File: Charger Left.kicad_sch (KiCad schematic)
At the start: 6 parts, among them Q1 AO4459, U1 CN3702

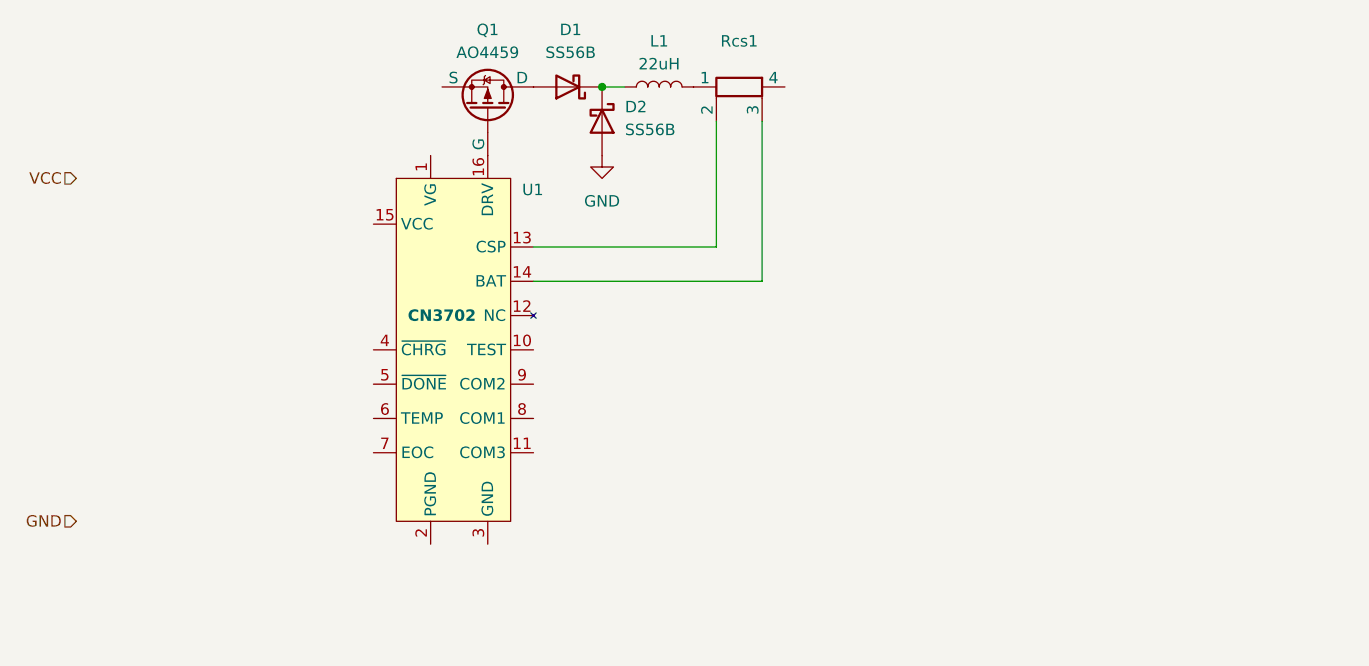
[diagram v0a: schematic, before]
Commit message: Add some resistors and caps
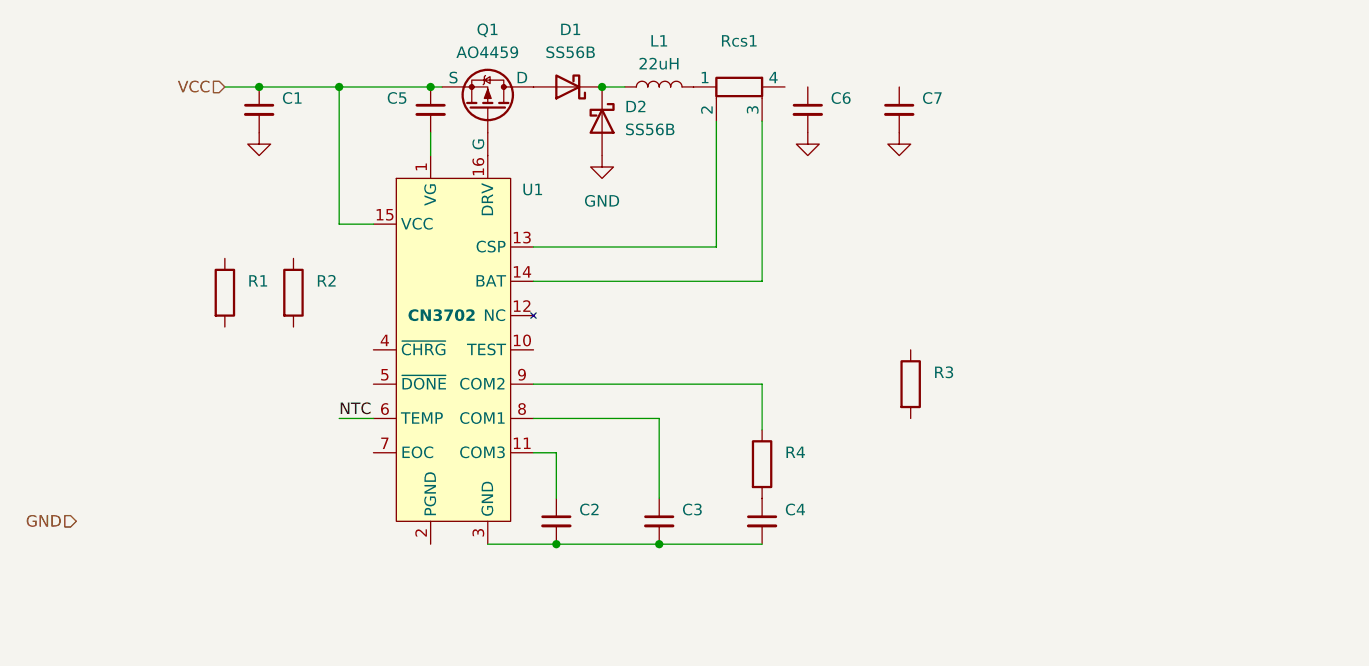
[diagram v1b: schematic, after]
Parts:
- added C1, C2, C3, C4, C5, C6, C7: (no value), symbol Device:C_Small
- added R1, R2, R3, R4: (no value), symbol Device:R
- Rcs1: footprint (none) -> BRAUNIT Charger:R_Shunt_2010_5025Metric
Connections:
- net GND: now also C1.2, C6.2, C7.2
- net VCC: now also Q1.1 (S), Q1.2 (S), Q1.3 (S), U1.15 (VCC), C1.1, C5.1
- net at U1.1 (VG): now also C5.2
- net at U1.11 (COM3): now also C2.1
- net at U1.3 (GND): now also C2.2, C3.2, C4.2
- net NTC: now reaches U1.6 (TEMP)
- net at U1.8 (COM1): now also C3.1
- net at U1.9 (COM2): now also R4.1
- new net: C4.1, R4.2

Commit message: Add BRAUNIT connector and battery detect/charge enable
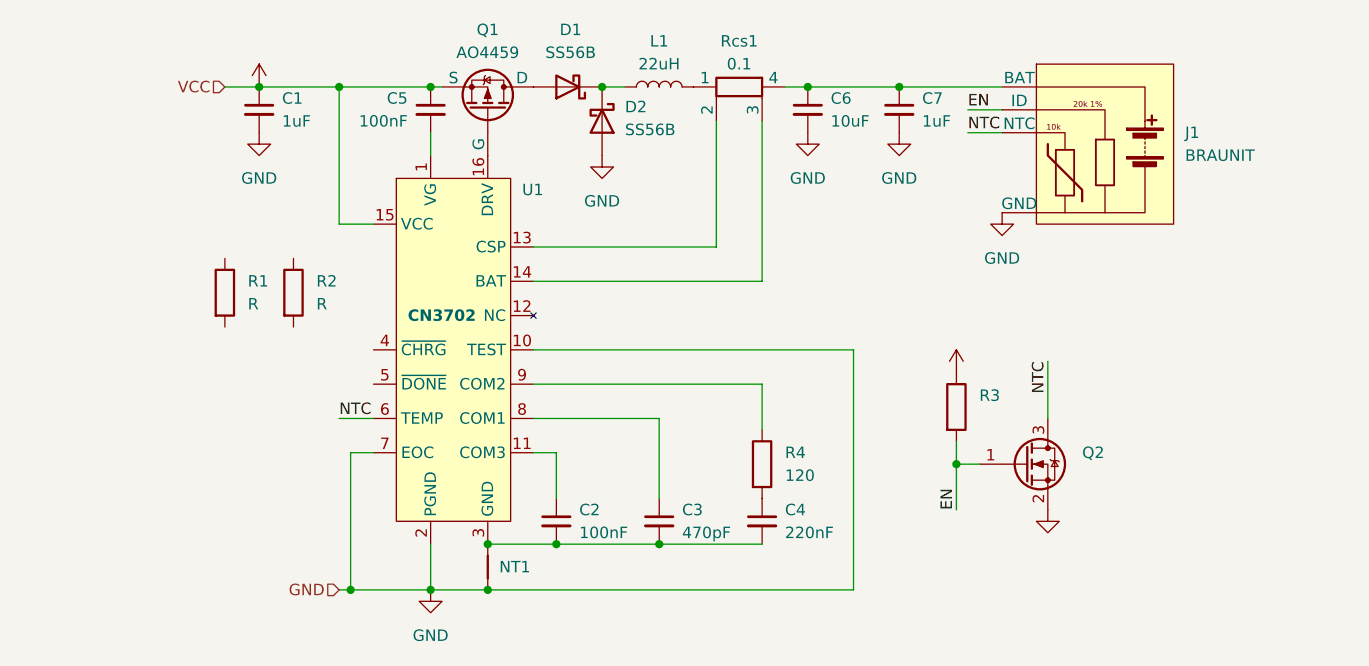
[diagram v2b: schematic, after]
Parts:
- added J1: BRAUNIT, BRAUNIT Charger:Blade_1x04_P2.5mm_Vertical_BRAUNIT_Loose, symbol BRAUNIT Charger:BRAUNIT
- added NT1: NetTie_2, NetTie:NetTie-2_SMD_Pad0.5mm, symbol Device:NetTie_2
- added Q2: (no value), symbol Transistor_FET:2N7002
- C1, C7: value (none) -> 1uF; footprint (none) -> Capacitor_SMD:C_0805_2012Metric
- C2, C5: value (none) -> 100nF; footprint (none) -> Capacitor_SMD:C_0805_2012Metric
- C3: value (none) -> 470pF; footprint (none) -> Capacitor_SMD:C_0805_2012Metric
- C4: value (none) -> 220nF; footprint (none) -> Capacitor_SMD:C_0805_2012Metric
- C6: value (none) -> 10uF; footprint (none) -> Capacitor_SMD:C_1206_3216Metric
- R1, R2: value (none) -> R
- R4: value (none) -> 120; footprint (none) -> Resistor_SMD:R_0805_2012Metric
- Rcs1: value (none) -> 0.1
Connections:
- net GND: now also U1.10 (TEST), U1.2 (PGND), U1.7 (EOC), J1.4 (GND), NT1.2, Q2.2 (S)
- net NTC: now also J1.3 (NTC), Q2.3 (D)
- net VCC: now also R3.1
- net at Rcs1.4: now also C6.1, C7.1, J1.1 (BAT)
- net EN: now reaches R3.2
- net EN: now also J1.2 (ID), Q2.1 (G)
- net at C2.2, C3.2, C4.2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: now also NT1.1
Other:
- moved on the sheet: R3

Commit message: Add LCSC part numbers for most components
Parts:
- removed D1, D2: SS56B, Diode_SMD:D_SMB, symbol BRAUNIT Charger:SS56B
- added D1, D2: (no value), symbol Device:D_Schottky
- added D3: LED_RAGB, symbol Device:LED_RAGB
- C1, C7: value 1uF -> (none); footprint Capacitor_SMD:C_0805_2012Metric -> (none); LCSC (none) -> C91185
- C2, C5: value 100nF -> (none); footprint Capacitor_SMD:C_0805_2012Metric -> (none); LCSC (none) -> C49678
- C3: value 470pF -> (none); footprint Capacitor_SMD:C_0805_2012Metric -> (none); LCSC (none) -> C107092
- C4: value 220nF -> (none); footprint Capacitor_SMD:C_0805_2012Metric -> (none); LCSC (none) -> C107131
- C6: value 10uF -> (none); footprint Capacitor_SMD:C_1206_3216Metric -> (none); LCSC (none) -> C109464
- J1: value BRAUNIT -> (none); footprint BRAUNIT Charger:Blade_1x04_P2.5mm_Vertical_BRAUNIT_Loose -> (none); now left out of the parts list
- L1: value 22uH -> (none); footprint Inductor_SMD:L_10.4x10.4_H4.8 -> (none); LCSC (none) -> C182173
- NT1: value NetTie_2 -> (none); footprint NetTie:NetTie-2_SMD_Pad0.5mm -> (none); now left out of the parts list
- Q1: value AO4459 -> (none); footprint Package_SO:SOIC-8_3.9x4.9mm_P1.27mm -> (none); LCSC (none) -> C49047
- Q2: LCSC (none) -> C8545
- R1: value R -> (none)
- R3: LCSC (none) -> C89104
- R4: value 120 -> (none); footprint Resistor_SMD:R_0805_2012Metric -> (none); LCSC (none) -> C114245
- Rcs1: value 0.1 -> (none); footprint BRAUNIT Charger:R_Shunt_2010_5025Metric -> (none); LCSC (none) -> C309644
- U1: value CN3702 -> (none); footprint Package_SO:TSSOP-16_4.4x5mm_P0.65mm -> (none); LCSC (none) -> C40655
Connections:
- net GND: now also D2.2 (A)
- net VCC: now also D3.2 (A)
- net at R2.1: now also D3.3 (GK)
- net at R2.2: now also U1.5 (~{DONE})
- net at L1.1: now also D1.1 (K), D2.1 (K)
- net at Q1.5 (D), Q1.6 (D), Q1.7 (D)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: now also D1.2 (A)
- net at R1.1: now also D3.1 (RK)
- net at R1.2: now also U1.4 (~{CHRG})
- no-connect marks 0 -> 1
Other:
- moved on the sheet: R1, R2

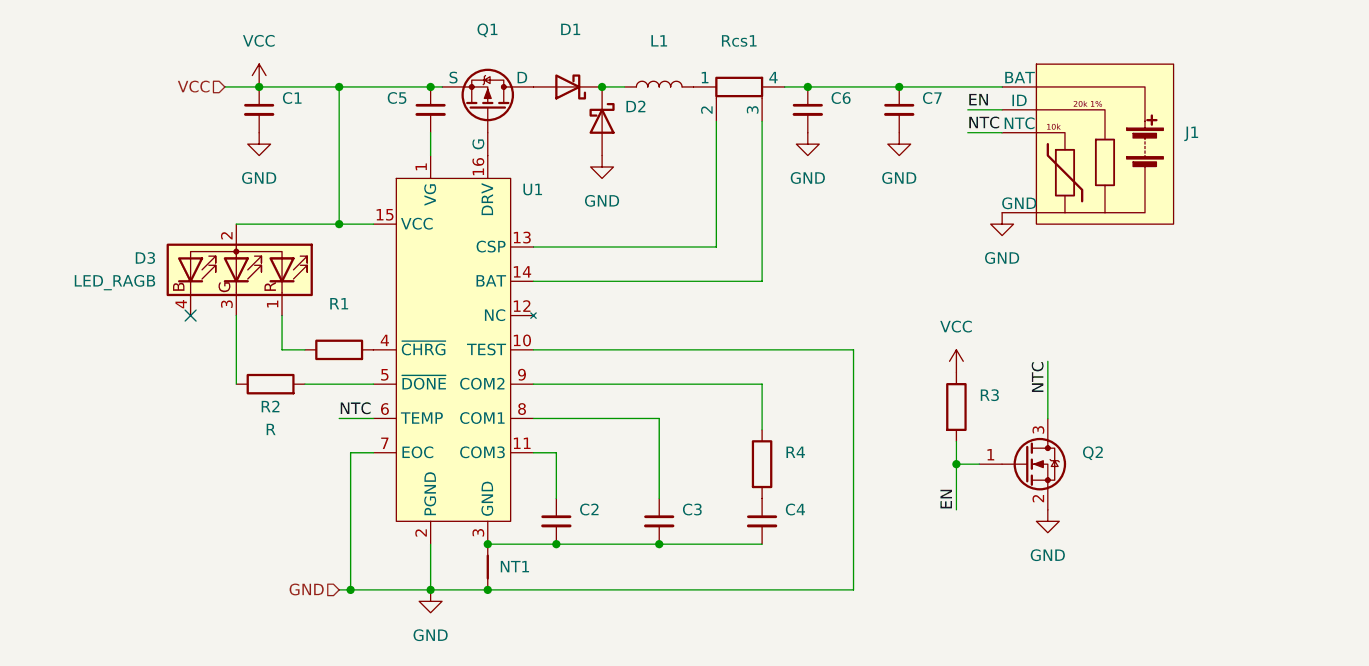
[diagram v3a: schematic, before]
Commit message: Add status indicator LED
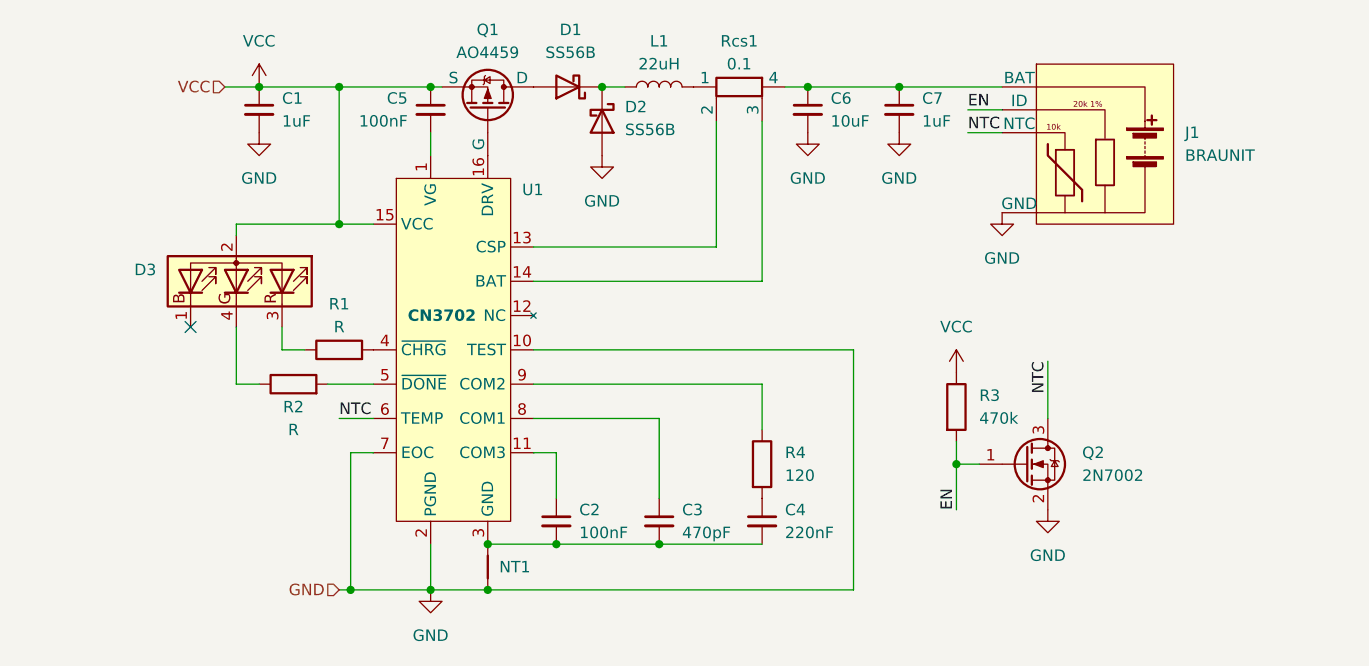
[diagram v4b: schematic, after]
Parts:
- removed D3: LED_RAGB, symbol Device:LED_RAGB
- added D3: (no value), symbol Device:LED_BARG
- C1, C7: value (none) -> 1uF; footprint (none) -> Capacitor_SMD:C_0805_2012Metric
- C2, C5: value (none) -> 100nF; footprint (none) -> Capacitor_SMD:C_0805_2012Metric
- C3: value (none) -> 470pF; footprint (none) -> Capacitor_SMD:C_0603_1608Metric
- C4: value (none) -> 220nF; footprint (none) -> Capacitor_SMD:C_0805_2012Metric
- C6: value (none) -> 10uF; footprint (none) -> Capacitor_SMD:C_1206_3216Metric
- D1, D2: value (none) -> SS56B; footprint (none) -> Diode_SMD:D_SMB
- J1: value (none) -> BRAUNIT; footprint (none) -> BRAUNIT Charger:Blade_1x04_P2.5mm_Vertical_BRAUNIT_Loose
- L1: value (none) -> 22uH; footprint (none) -> Inductor_SMD:L_10.4x10.4_H4.8
- NT1: value (none) -> NetTie_2; footprint (none) -> NetTie:NetTie-2_SMD_Pad0.5mm
- Q1: value (none) -> AO4459; footprint (none) -> Package_SO:SOIC-8_3.9x4.9mm_P1.27mm
- Q2: value (none) -> 2N7002; footprint (none) -> Package_TO_SOT_SMD:SOT-23
- R1: value (none) -> R
- R3: value (none) -> 470k; footprint (none) -> Resistor_SMD:R_0805_2012Metric
- R4: value (none) -> 120; footprint (none) -> Resistor_SMD:R_0805_2012Metric
- Rcs1: value (none) -> 0.1; footprint (none) -> BRAUNIT Charger:R_Shunt_2010_5025Metric
- U1: value (none) -> CN3702; footprint (none) -> Package_SO:TSSOP-16_4.4x5mm_P0.65mm
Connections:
- net VCC: now also D3.2 (A)
- net at R2.1: now also D3.4 (GK)
- net at R1.1: now also D3.3 (RK)
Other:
- moved on the sheet: R2

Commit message: Specify LED, resistors, and start on USB-C circuit
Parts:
- D3: value (none) -> MHS110RGBCT; footprint (none) -> BRAUNIT Charger:LED_RGB_Meihua_MHS110RGBCT
- R1, R2: value R -> 2k7; footprint (none) -> Resistor_SMD:R_0603_1608Metric; LCSC (none) -> C114612
- Rcs1: value 0.1 -> 0R1

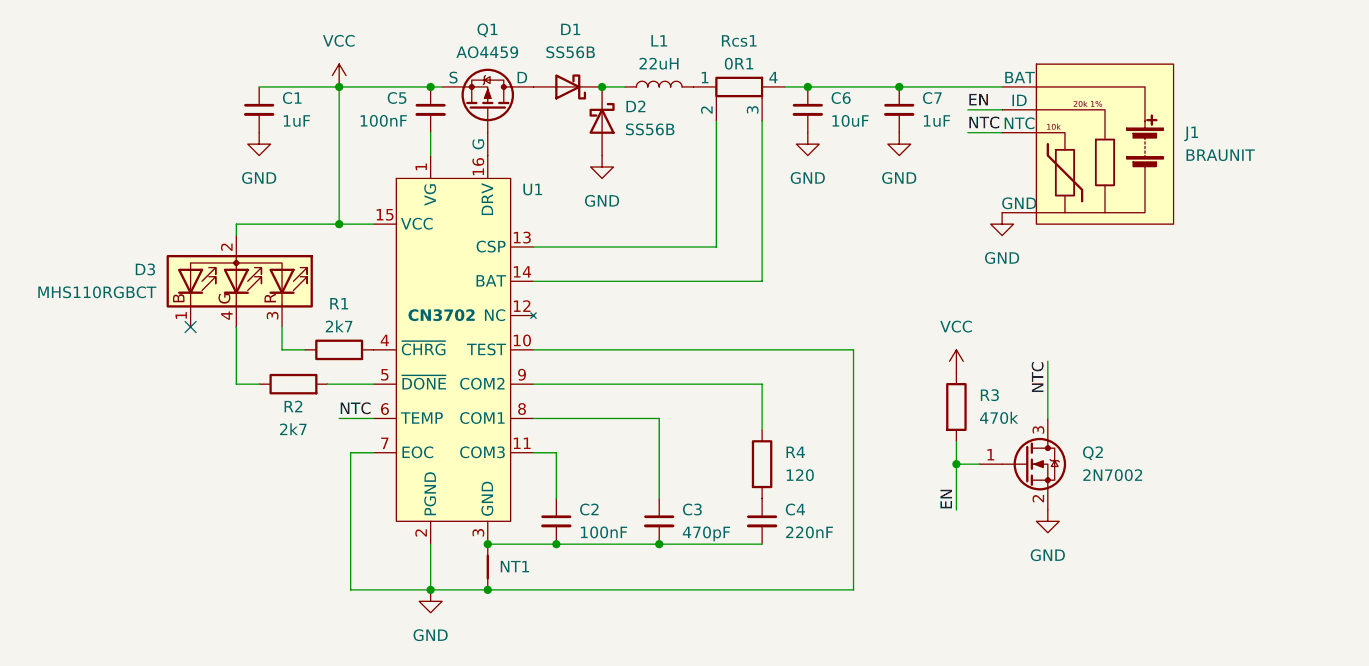
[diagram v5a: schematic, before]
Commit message: Add ESD protection, I2C header, and specify passives
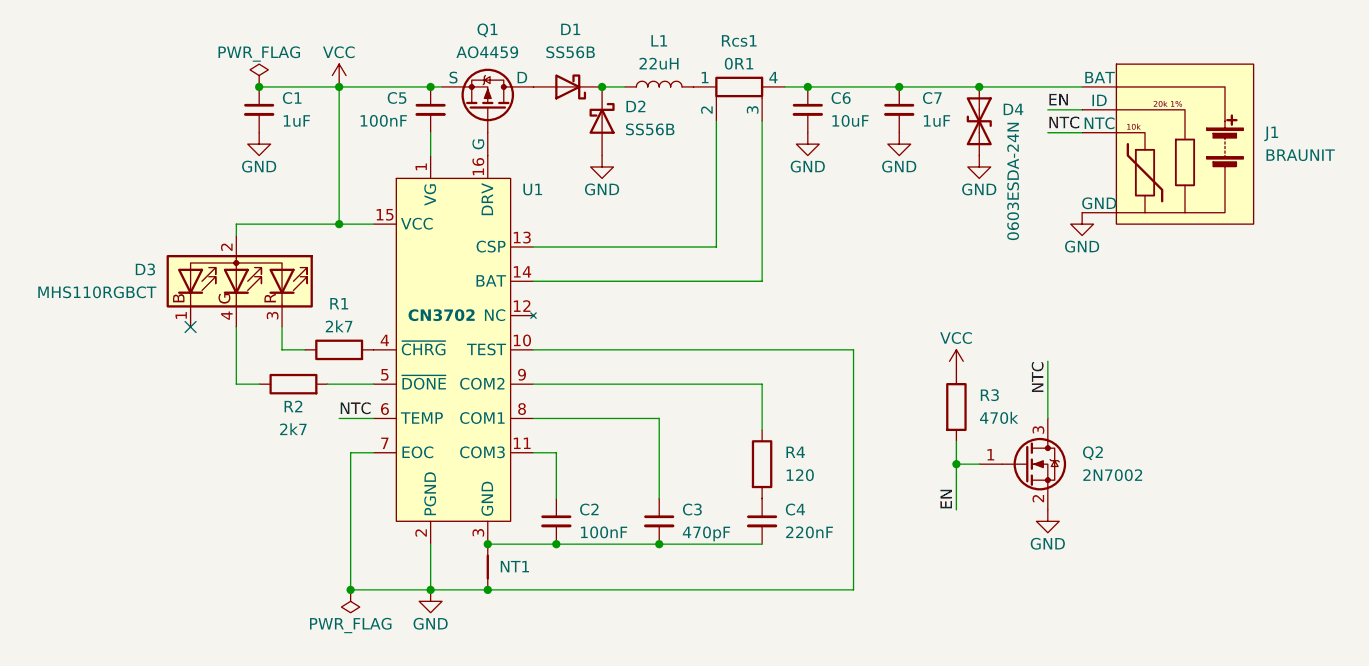
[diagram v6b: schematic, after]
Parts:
- added D4: 0603ESDA-24N, Diode_SMD:D_0603_1608Metric, symbol Device:D_TVS
- C2, C5: footprint Capacitor_SMD:C_0805_2012Metric -> Capacitor_SMD:C_0603_1608Metric; LCSC C49678 -> C14663
- C4: footprint Capacitor_SMD:C_0805_2012Metric -> Capacitor_SMD:C_0603_1608Metric; LCSC C107131 -> C107083
- R3: footprint Resistor_SMD:R_0805_2012Metric -> Resistor_SMD:R_0603_1608Metric; LCSC C89104 -> C114622
- R4: footprint Resistor_SMD:R_0805_2012Metric -> Resistor_SMD:R_0603_1608Metric; LCSC C114245 -> C114640
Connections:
- net GND: now also D4.2 (A2)
- net at C6.1, C7.1, J1.1 (BAT)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: now also D4.1 (A1)
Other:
- moved on the sheet: J1

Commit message: Initial board layout
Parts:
- L1: footprint Inductor_SMD:L_10.4x10.4_H4.8 -> BRAUNIT Charger:L_Sunltech_SLO0630H; LCSC C182173 -> C207843
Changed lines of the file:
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@@
     (property "Reference" "L1" (id 0) (at 149.86 67.31 90))
     (property "Value" "22uH" (id 1) (at 149.86 69.85 90))
-    (property "Footprint" "Inductor_SMD:L_10.4x10.4_H4.8" (id 2) (at 149.86 72.39 0)
+    (property "Footprint" "BRAUNIT Charger:L_Sunltech_SLO0630H" (id 2) (at 149.86 72.39 0)
       (effects (font (size 1.27 1.27)) hide)
     )
@@
       (effects (font (size 1.27 1.27)) hide)
     )
-    (property "LCSC" "C182173" (id 4) (at 149.86 72.39 90)
+    (property "LCSC" "C207843" (id 4) (at 149.86 72.39 90)
       (effects (font (size 1.27 1.27)) hide)
     )
